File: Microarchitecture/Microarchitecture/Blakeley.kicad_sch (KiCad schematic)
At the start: 11 parts

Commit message: Updated timing diagrams, etc, control fsm and verified workings
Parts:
- removed AND(W-1)1, AND6, AND7: ~, symbol Symbols:AND
- removed MUX5: ~, symbol Symbols:MUX
- added 3AND1, 3AND2, 3ANDW: ~, symbol Symbols:AND3
- added ADD: ~, symbol Symbols:ADD
- added DECODE1: ~, symbol Symbols:DECODE
- added REG5: ~, symbol Symbols:REG
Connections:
- net A: now also 3AND1. (AND3), 3AND2. (AND3), 3ANDW. (AND3)
- net B: now also 3AND1. (AND3), 3AND2. (AND3), 3ANDW. (AND3)
- net N: now also SUB2. (DIN1[W-1...0]); no longer SUB2.2 (DIN1[W-1...0])
- net R: now also SHIFT3. (DOUT[W-1...0]); no longer SHIFT3.1 (DIN[W-1...0])
- net SUMDMUX_C0: now also DMUX2. (DMUX1[W-1...0]); no longer DMUX2.4 (C0)
- net SUMMUX_C0: now also MUX6. (MUX[W-1...0]); no longer MUX6.4 (C0)
- new net: ADD. (DIN1[log2(W)-1...0]), REG5. (RST)
- new net: 3AND1. (AND3), 3AND2. (AND3), 3ANDW. (AND3), DECODE1. (D[W-1...0])
- new net: 3AND1. (AND3), 3AND2. (AND3), 3ANDW. (AND3), ADD1. (DIN1[W-1...0])
- new net: ADD1. (DIN1[W-1...0]), SHIFT3. (DOUT[W-1...0])
- new net: ADD1. (DIN1[W-1...0]), MUX6. (MUX[W-1...0])
- new net: MUX6. (MUX[W-1...0]), SUB2. (DIN1[W-1...0])
- new net: MUX6. (MUX[W-1...0]), REG10. (RST)
- new net: DMUX2. (DMUX1[W-1...0]), REG11. (RST)
- new net: DMUX2. (DMUX1[W-1...0]), SUB2. (DIN1[W-1...0])
- new net '1': ADD. (DIN1[log2(W)-1...0])
- new net ADEC: ADD. (DIN1[log2(W)-1...0]), DECODE1. (D[W-1...0]), REG5. (RST)
- new net ADEC_CLK: REG5. (RST)
- new net ADEC_RST: REG5. (RST)
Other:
- note added: "From RSA_MODULE"
- note added: "From rsa_regio"
- note added: "NB: NOTE1"
- note added: "NOTE1: DECODER The decoder has to be implemented inversely. This means that when the decoder gets input '0xFF' the decoded output has to be '0x0'. This is to ensure the MSB scanning of the A line and the bitwize mul with the whole B."
- note added: "To RSA_MODULE"
- moved on the sheet: REG10, REG11

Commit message: Latest changes
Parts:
- renumbered 3AND2 to 3AND7, 3AND1 to 3AND8, 3ANDW to 3ANDW2, ADD to ADD8, ADD1 to ADD9, DECODE1 to DECODE4, DMUX2 to DMUX5, MUX6 to MUX11, REG5 to REG18, REG10 to REG19, REG11 to REG20, SHIFT3 to SHIFT5, SUB2 to SUB5
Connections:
- net at ADD9. (DIN1[W-1...0]): now also MUX11. (MUX[W-1...0]); no longer SHIFT5. (DOUT[W-1...0])
- new net: ADD8. (DIN1[log2(W)-1...0]), REG18. (RST)
- new net: 3AND7. (AND3), 3AND8. (AND3), 3ANDW2. (AND3), DECODE4. (D[W-1...0])
- new net: 3AND7. (AND3), 3AND8. (AND3), 3ANDW2. (AND3), ADD9. (DIN1[W-1...0])
- new net: ADD9. (DIN1[W-1...0]), SHIFT5. (DOUT[W-1...0])
- new net: MUX11. (MUX[W-1...0]), SUB5. (DIN1[W-1...0])
- new net: MUX11. (MUX[W-1...0]), REG19. (RST)
- new net: DMUX5. (DMUX1[W-1...0]), REG20. (RST)
- new net: DMUX5. (DMUX1[W-1...0]), SUB5. (DIN1[W-1...0])

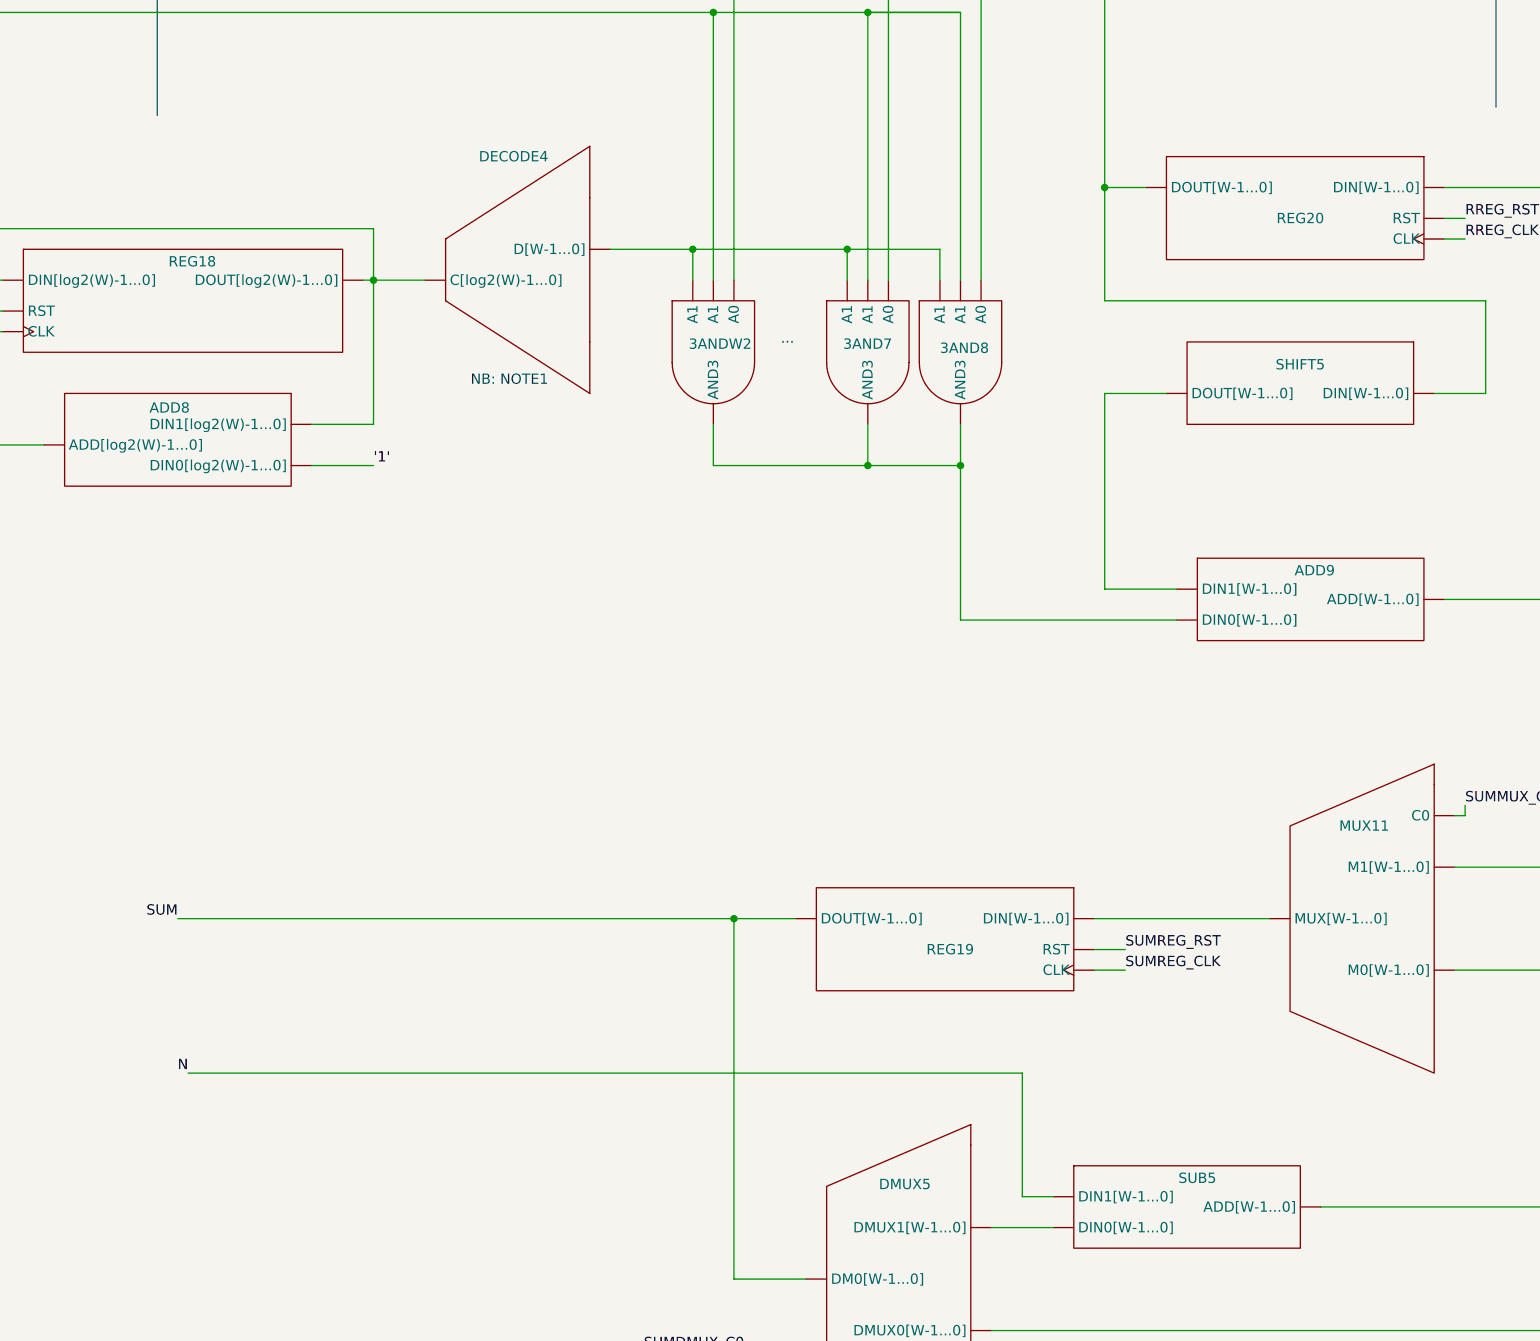
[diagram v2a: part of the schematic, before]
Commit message: Added rev2 BLAKELEY_MODULE
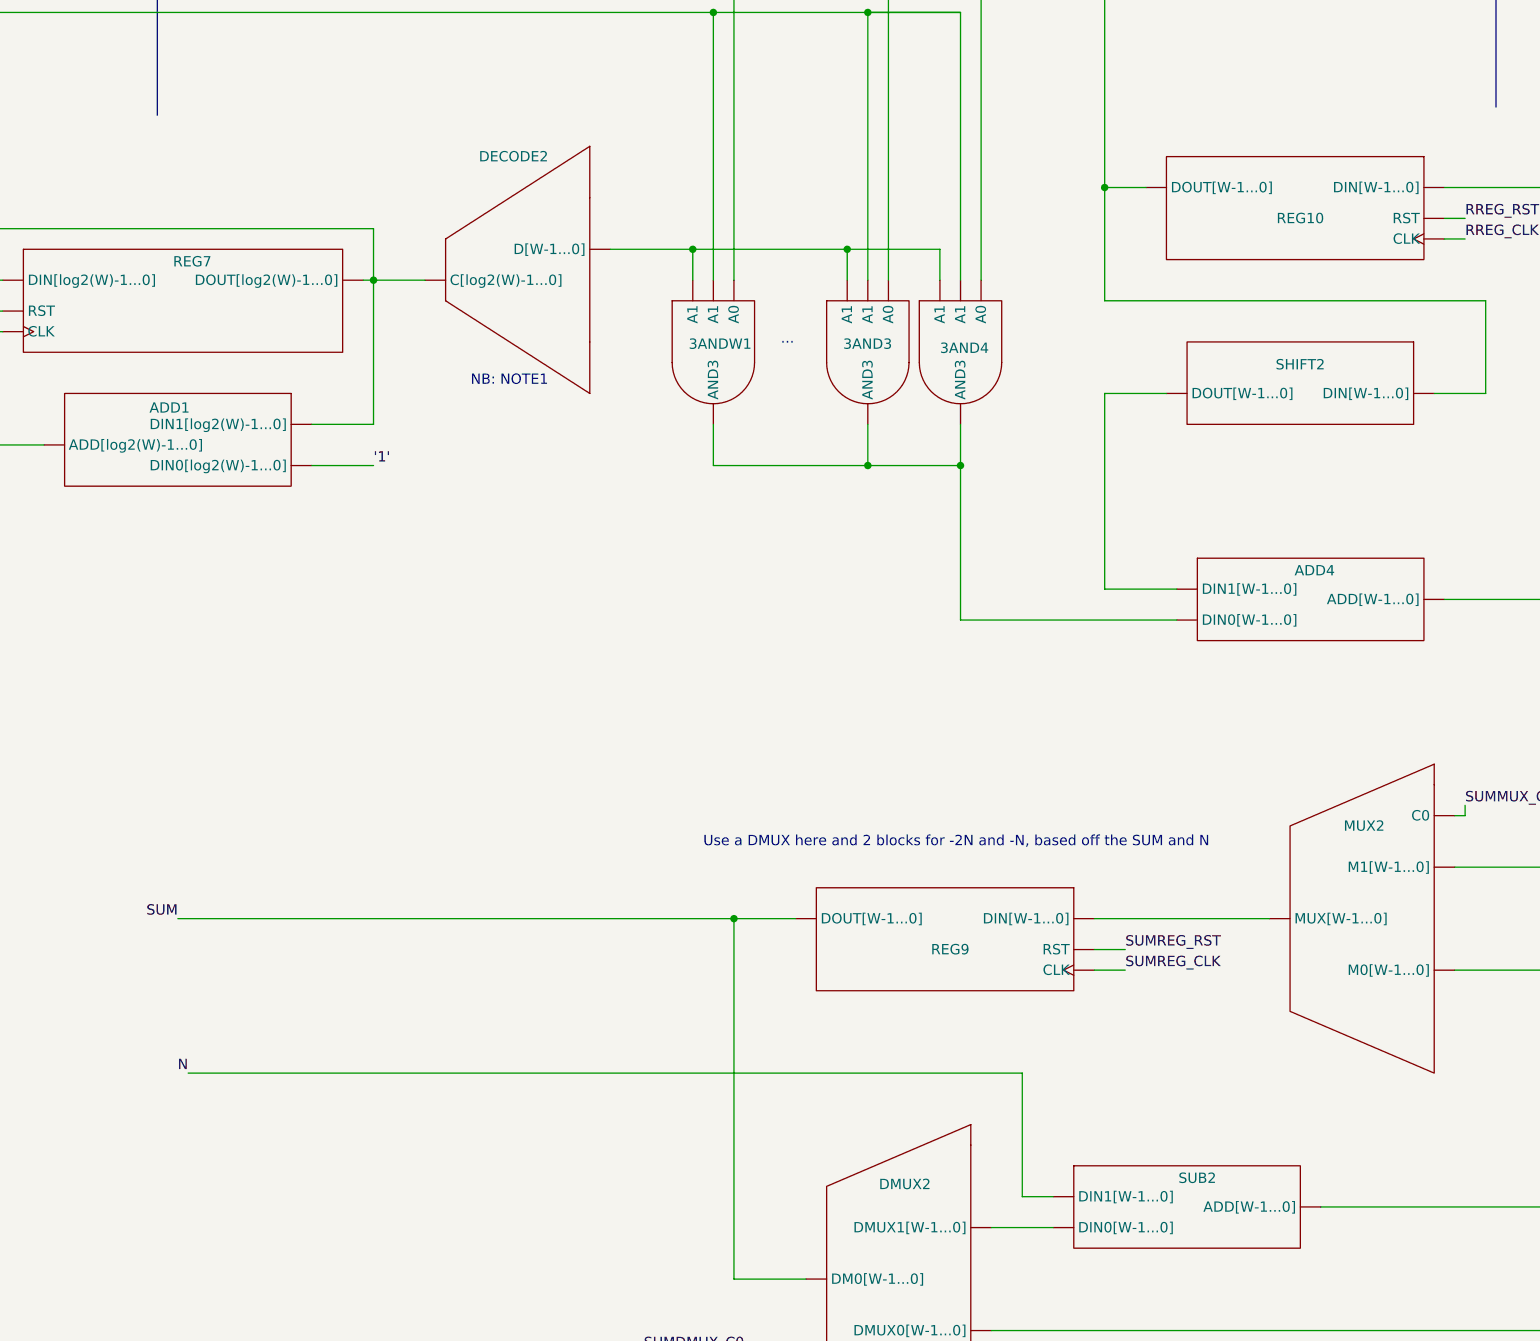
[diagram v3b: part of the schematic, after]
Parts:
- renumbered 3AND7 to 3AND3, 3AND8 to 3AND4, 3ANDW2 to 3ANDW1, ADD8 to ADD1, ADD9 to ADD4, DECODE4 to DECODE2, DMUX5 to DMUX2, MUX11 to MUX2, REG20 to REG10, REG18 to REG7, REG19 to REG9, SHIFT5 to SHIFT2, SUB5 to SUB2
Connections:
- net at ADD4. (DIN1[W-1...0]): now also MUX2. (MUX[W-1...0]); no longer SHIFT2. (DOUT[W-1...0])
- new net: ADD1. (DIN1[log2(W)-1...0]), REG7. (RST)
- new net: 3AND3. (AND3), 3AND4. (AND3), 3ANDW1. (AND3), DECODE2. (D[W-1...0])
- new net: 3AND3. (AND3), 3AND4. (AND3), 3ANDW1. (AND3), ADD4. (DIN1[W-1...0])
- new net: ADD4. (DIN1[W-1...0]), SHIFT2. (DOUT[W-1...0])
- new net: MUX2. (MUX[W-1...0]), SUB2. (DIN1[W-1...0])
- new net: MUX2. (MUX[W-1...0]), REG9. (RST)
- new net: DMUX2. (DMUX1[W-1...0]), REG10. (RST)
- new net: DMUX2. (DMUX1[W-1...0]), SUB2. (DIN1[W-1...0])
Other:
- note added: "Use a DMUX here and 2 blocks for -2N and -N, based off the SUM and N"

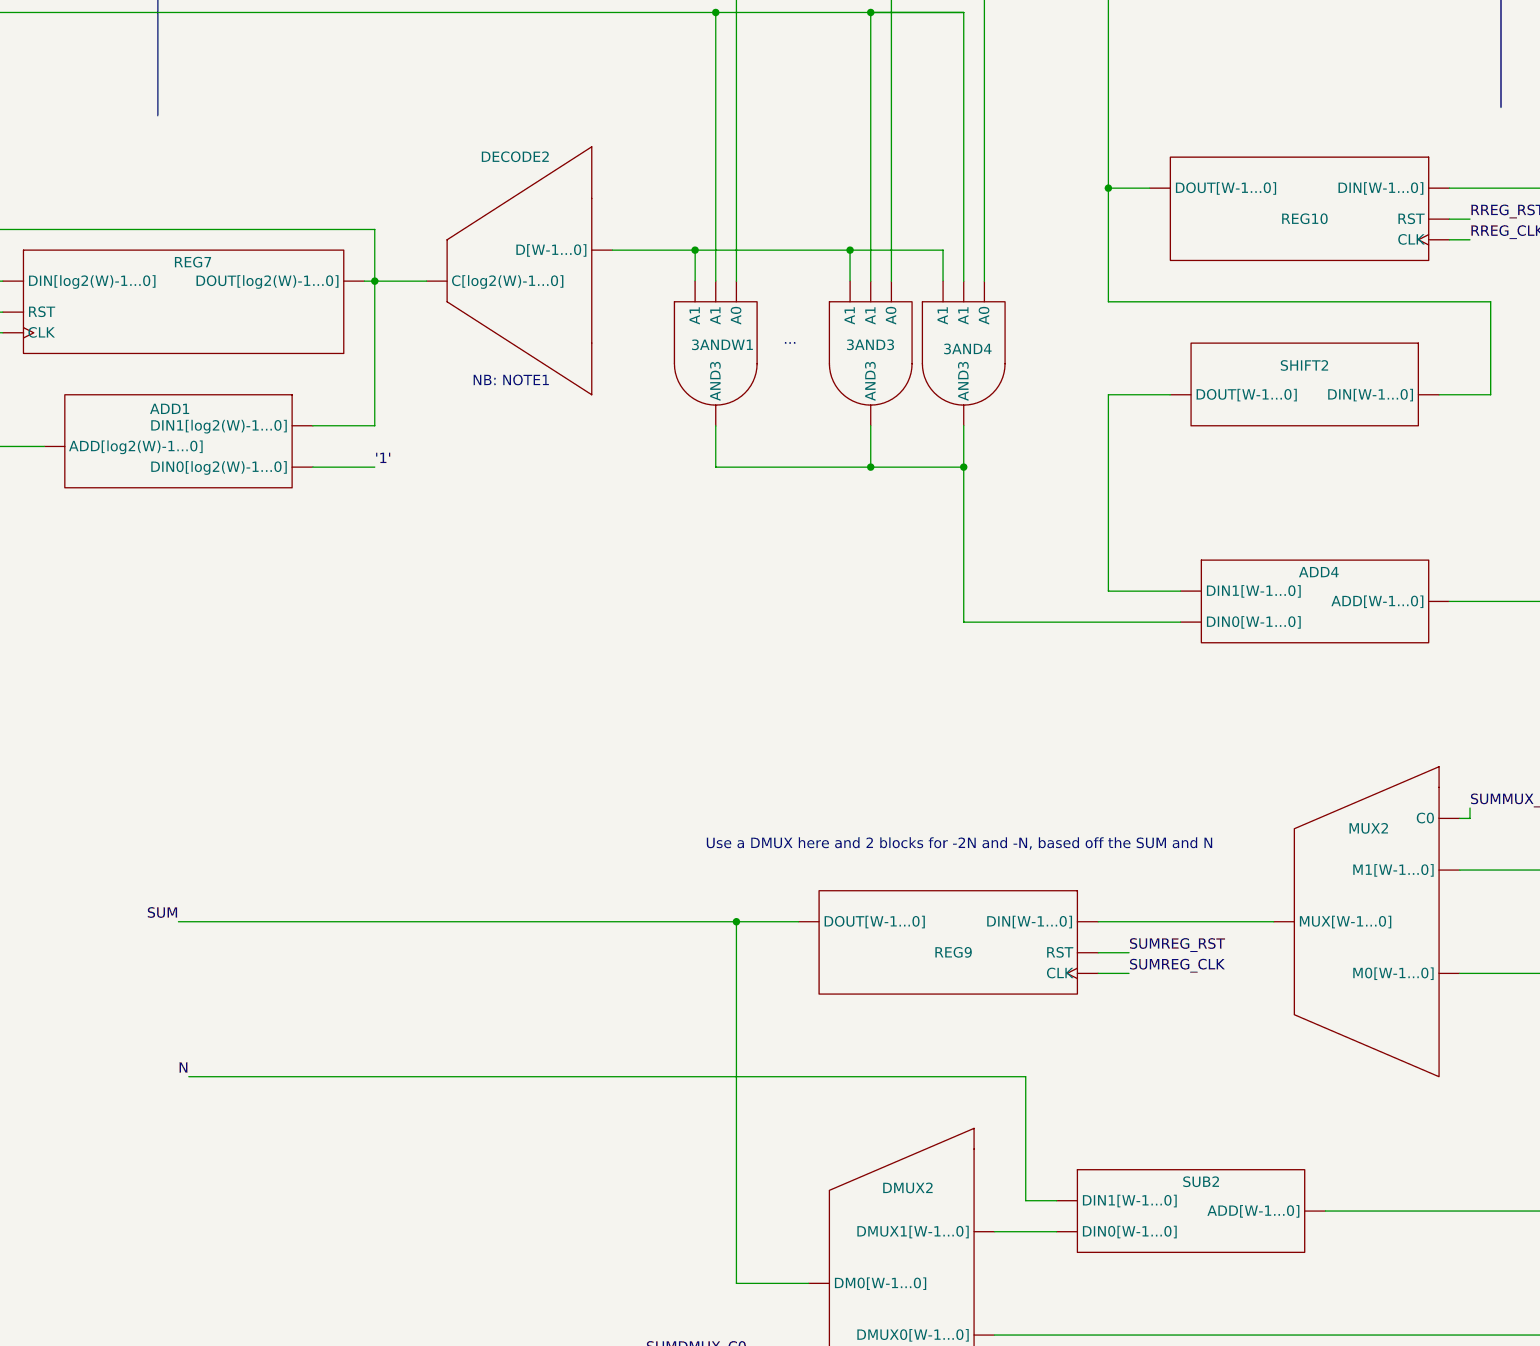
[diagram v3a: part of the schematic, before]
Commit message: Blakeley datapath working
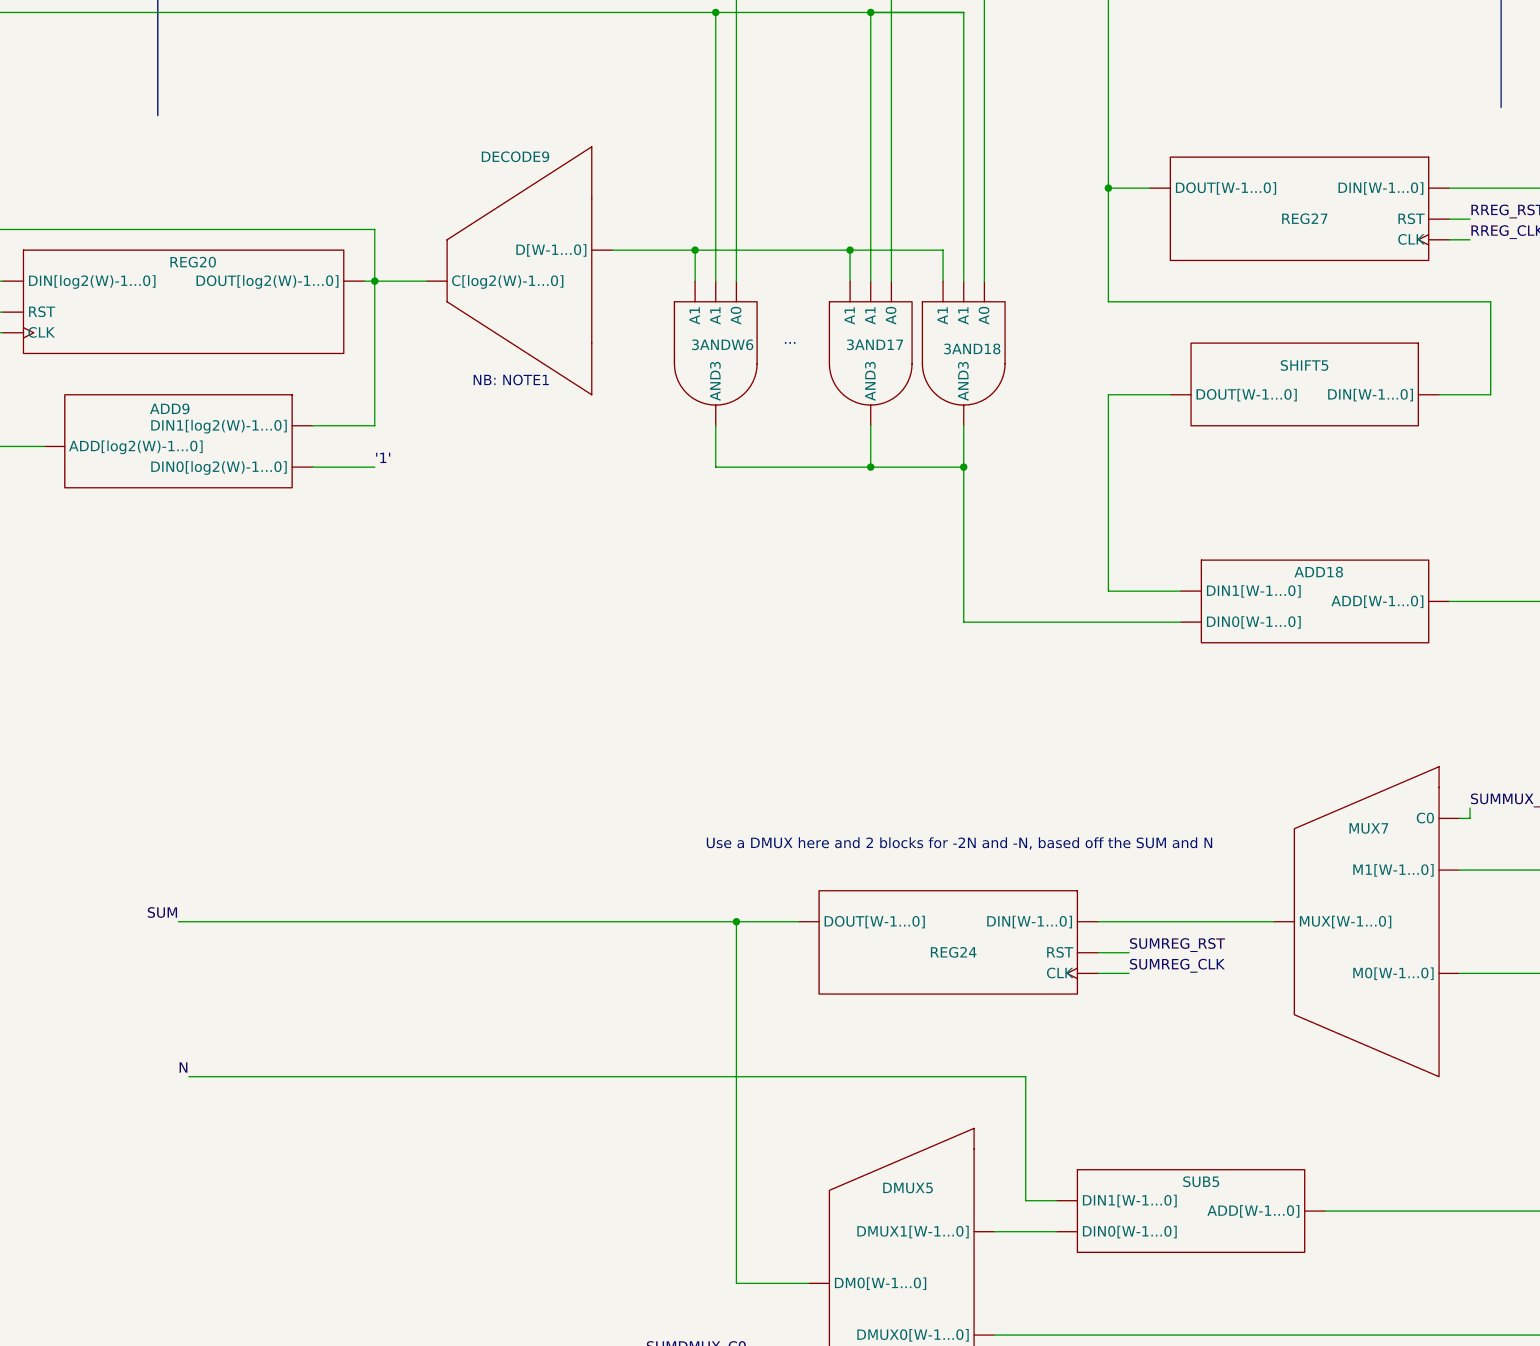
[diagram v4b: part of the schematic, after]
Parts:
- renumbered 3AND3 to 3AND17, 3AND4 to 3AND18, 3ANDW1 to 3ANDW6, ADD4 to ADD18, ADD1 to ADD9, DECODE2 to DECODE9, DMUX2 to DMUX5, MUX2 to MUX7, REG7 to REG20, REG9 to REG24, REG10 to REG27, SHIFT2 to SHIFT5, SUB2 to SUB5
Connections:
- net at ADD18. (DIN1[W-1...0]): now also MUX7. (MUX[W-1...0]); no longer SHIFT5. (DOUT[W-1...0])
- new net: ADD9. (DIN1[log2(W)-1...0]), REG20. (RST)
- new net: 3AND17. (AND3), 3AND18. (AND3), 3ANDW6. (AND3), DECODE9. (D[W-1...0])
- new net: 3AND17. (AND3), 3AND18. (AND3), 3ANDW6. (AND3), ADD18. (DIN1[W-1...0])
- new net: ADD18. (DIN1[W-1...0]), SHIFT5. (DOUT[W-1...0])
- new net: MUX7. (MUX[W-1...0]), SUB5. (DIN1[W-1...0])
- new net: MUX7. (MUX[W-1...0]), REG24. (RST)
- new net: DMUX5. (DMUX1[W-1...0]), REG27. (RST)
- new net: DMUX5. (DMUX1[W-1...0]), SUB5. (DIN1[W-1...0])
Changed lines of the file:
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@@
 		(on_board yes)
 		(dnp no)
-		(property "Reference" "REG7"
+		(property "Reference" "REG20"
 			(at 202.438 84.074 0)
 			(effects
@@
 		(on_board yes)
 		(dnp no)
-		(property "Reference" "3AND4"
+		(property "Reference" "3AND18"
 			(at 294.64 94.742 0)
 			(effects
@@
 		(on_board yes)
 		(dnp no)
-		(property "Reference" "SHIFT2"
+		(property "Reference" "SHIFT5"
 			(at 339.09 96.774 0)
 			(effects
@@
 		(on_board yes)
 		(dnp no)
-		(property "Reference" "DECODE2"
+		(property "Reference" "DECODE9"
 			(at 242.062 71.12 0)
 			(effects
@@
 		(on_board yes)
 		(dnp no)
-		(property "Reference" "ADD4"
+		(property "Reference" "ADD18"
 			(at 340.868 122.174 0)
 			(effects
@@
 		(on_board yes)
 		(dnp no)
-		(property "Reference" "3AND3"
+		(property "Reference" "3AND17"
 			(at 282.702 94.234 0)
 			(effects
@@
 		(on_board yes)
 		(dnp no)
-		(property "Reference" "MUX2"
+		(property "Reference" "MUX7"
 			(at 346.964 153.67 0)
 			(effects
@@
 		(on_board yes)
 		(dnp no)
-		(property "Reference" "REG10"
+		(property "Reference" "REG27"
 			(at 339.09 78.74 0)
 			(effects
@@
 		(on_board yes)
 		(dnp no)
-		(property "Reference" "3ANDW1"
+		(property "Reference" "3ANDW6"
 			(at 263.652 94.234 0)
 			(effects
@@
 		(on_board yes)
 		(dnp no)
-		(property "Reference" "ADD1"
+		(property "Reference" "ADD9"
 			(at 199.644 102.108 0)
 			(effects
@@
 		(on_board yes)
 		(dnp no)
-		(property "Reference" "SUB2"
+		(property "Reference" "SUB5"
 			(at 326.39 197.104 0)
 			(effects
@@
 		(on_board yes)
 		(dnp no)
-		(property "Reference" "DMUX2"
+		(property "Reference" "DMUX5"
 			(at 290.322 197.866 0)
 			(effects
@@
 		(on_board yes)
 		(dnp no)
-		(property "Reference" "REG9"
+		(property "Reference" "REG24"
 			(at 295.91 168.91 0)
 			(effects
